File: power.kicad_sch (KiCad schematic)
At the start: 63 parts, among them Q1 AO3401A, Q2 AO3401A, Q21 FS8205A, Q6 2N7002, U10 BQ27546, U27 TPS63001, U29 BQ24081, U30 DW01+G, U6 TPS61040DBV

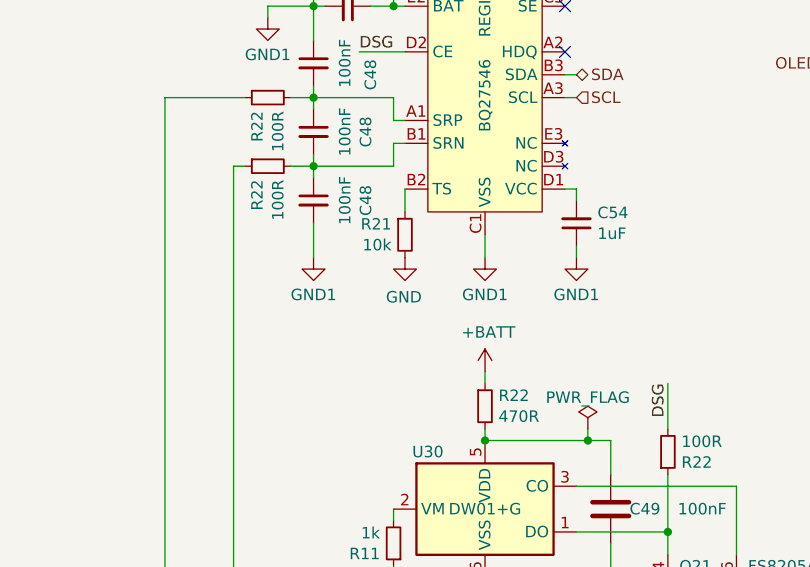
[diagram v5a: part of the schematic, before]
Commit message: Fix fuel gauge thermistor ground reference
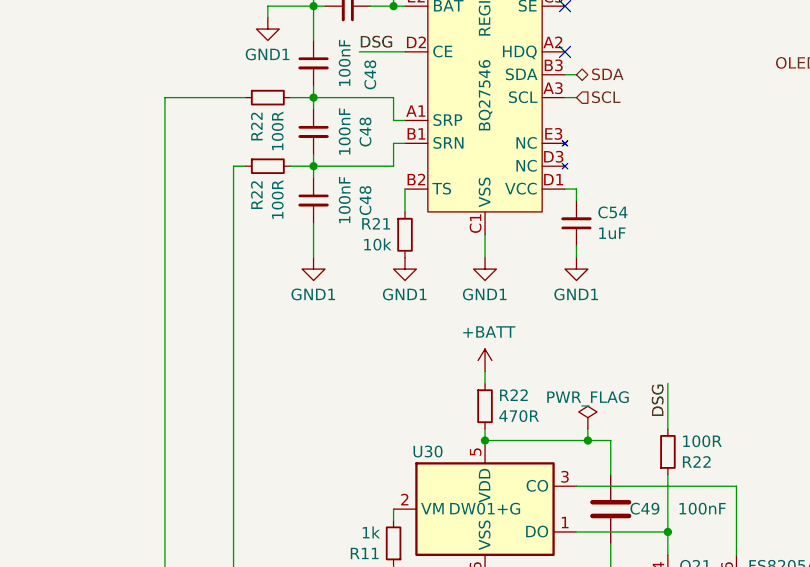
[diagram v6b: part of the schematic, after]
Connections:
- net GND: no longer R21.2
- net GND1: now also R21.2
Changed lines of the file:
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@@
+    )
+  )
+  (symbol (lib_id "power:GND1") (at 128.27 123.19 0) (unit 1)
+    (in_bom yes) (on_board yes) (dnp no) (fields_autoplaced)
+    (property "Reference" "#PWR035" (at 128.27 129.54 0)
+      (effects (font (size 1.27 1.27)) hide)
+    )
+    (property "Value" "GND1" (at 128.27 127.3255 0)
+      (effects (font (size 1.27 1.27)))
+    )
+    (property "Footprint" "" (at 128.27 123.19 0)
+      (effects (font (size 1.27 1.27)) hide)
+    )
+    (property "Datasheet" "" (at 128.27 123.19 0)
+      (effects (font (size 1.27 1.27)) hide)
+    )
+    (pin "1")
+    (instances
+      (project "oled-nametag"
+        (path "/c0b8a503-1da4-4e1a-941c-dddf39a5c519/b1f1b085-615b-4d75-b80e-4b089a5e74f7"
+          (reference "#PWR035") (unit 1)
+        )
+      )
     )
   )
@@
         )
       )
-    )
-  )
-  (symbol (lib_id "power:GND") (at 128.27 123.19 0) (mirror y) (unit 1)
-    (in_bom yes) (on_board yes) (dnp no)
-    (property "Reference" "#PWR0210" (at 128.27 129.54 0)
-      (effects (font (size 1.27 1.27)) hide)
-    )
-    (property "Value" "GND" (at 128.143 127.5842 0)
-      (effects (font (size 1.27 1.27)))
-    )
-    (property "Footprint" "" (at 128.27 123.19 0)
-      (effects (font (size 1.27 1.27)) hide)
-    )
-    (property "Datasheet" "" (at 128.27 123.19 0)
-      (effects (font (size 1.27 1.27)) hide)
-    )
-    (pin "1")
-    (instances
-      (project "rgb-led-nametag-48x16"
-        (path "/751d823e-1d7b-4501-9658-d06d459b0e16"
-          (reference "#PWR0210") (unit 1)
-        )
-      )
-      (project "oled-nametag"
-        (path "/c0b8a503-1da4-4e1a-941c-dddf39a5c519/b1f1b085-615b-4d75-b80e-4b089a5e74f7"
-          (reference "#PWR035") (unit 1)
-        )
-      )

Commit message: Add missing LCSC partnumbers
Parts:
- Q1, Q2: LCSC (none) -> C15127
- Q6: LCSC (none) -> C8545
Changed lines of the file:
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@@
       (effects (font (size 1.27 1.27)) (justify left) hide)
+    )
+    (property "LCSC" "C15127" (at 158.75 49.53 90)
+      (effects (font (size 1.27 1.27)) hide)
     )
     (pin "1")
@@
     (property "Datasheet" "http://www.aosmd.com/pdfs/datasheet/AO3401A.pdf" (at 194.31 85.09 0)
       (effects (font (size 1.27 1.27)) (justify left) hide)
+    )
+    (property "LCSC" "C15127" (at 194.31 85.09 90)
+      (effects (font (size 1.27 1.27)) hide)
     )
     (pin "1")
@@
       (effects (font (size 1.27 1.27)) (justify left) hide)
     )
-    (pin "1")
+    (property "LCSC" "C8545" (at 191.77 101.6 0)
+      (effects (font (size 1.27 1.27)) hide)
+    )
+    (pin "1")

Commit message: Adjust to new JLC manufacturing requirements
Change default minimum via hole size to .3mm
Replace package thermal vias by .3mm via
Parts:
- U27, U29: footprint Package_SON:Texas_DRC0010J_ThermalVias -> Package_Texas:Texas_DRC0010J_ThermalVias.3
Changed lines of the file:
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@@
       (effects (font (size 1.27 1.27)))
     )
-    (property "Footprint" "Package_SON:Texas_DRC0010J_ThermalVias" (at 248.92 66.04 0)
+    (property "Footprint" "Package_Texas:Texas_DRC0010J_ThermalVias.3" (at 248.92 66.04 0)
       (effects (font (size 1.27 1.27)) hide)
     )
@@
       (effects (font (size 1.27 1.27)))
     )
-    (property "Footprint" "Package_SON:Texas_DRC0010J_ThermalVias" (at 66.04 49.53 0)
-      (effects (font (size 1.27 1.27)) hide)
-    )
+    (property "Footprint" "Package_Texas:Texas_DRC0010J_ThermalVias.3" (at 66.04 49.53 0)
+      (effects (font (size 1.27 1.27)) hide)
+    )
